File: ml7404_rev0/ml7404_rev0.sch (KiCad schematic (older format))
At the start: 97 parts, among them CN1 MHF-SW23, 20549-001E, CN2 MHF1, 20279-001E-03, U1 SKY13438-374LF, U2 ML7404, U3 BRCB032GWZ-3, U4 BH18PB1WFV

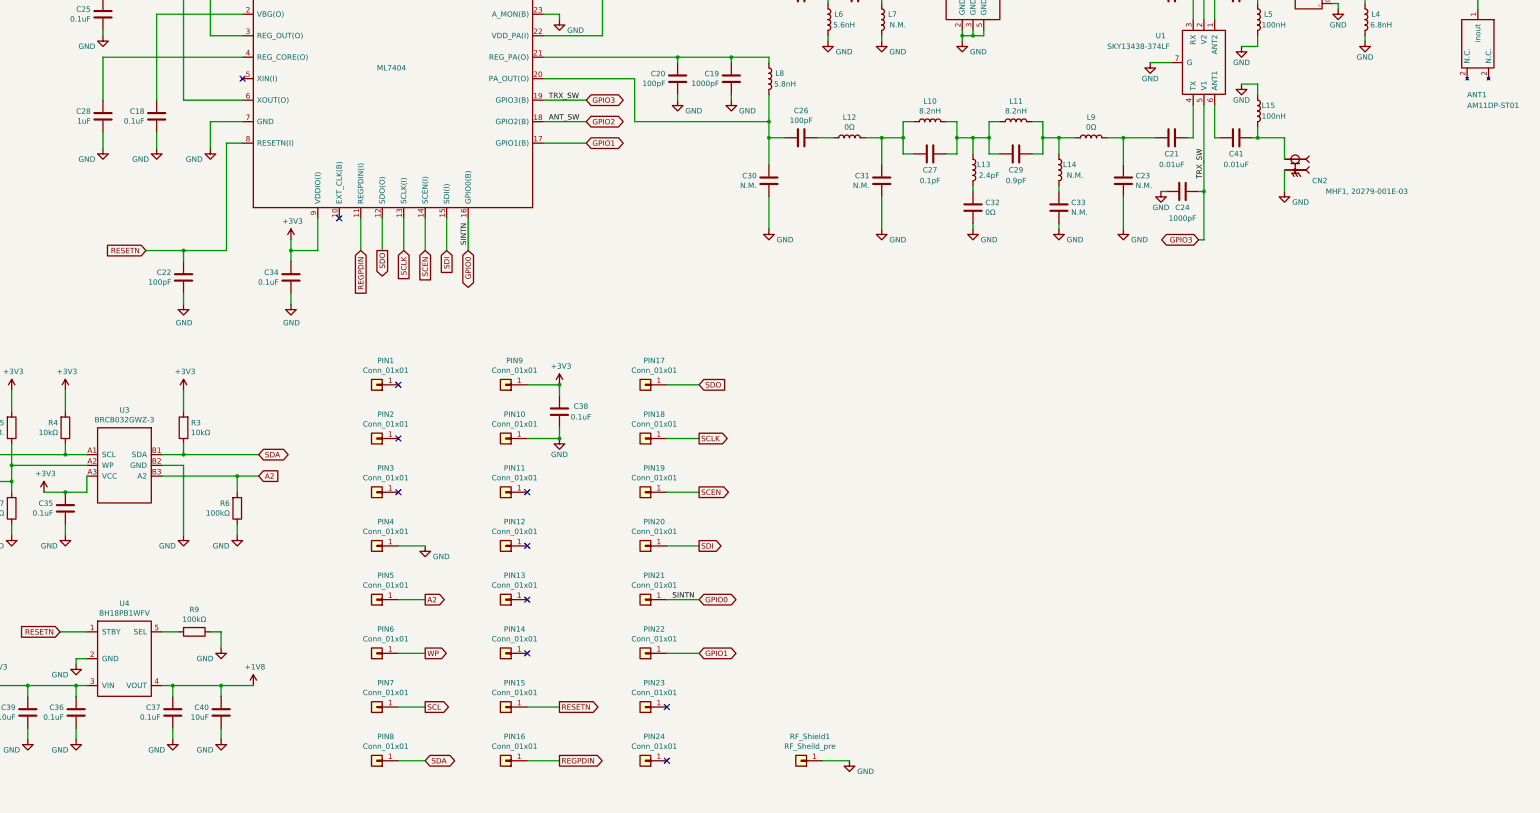
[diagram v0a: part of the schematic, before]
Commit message: adjusted RF shield footprint
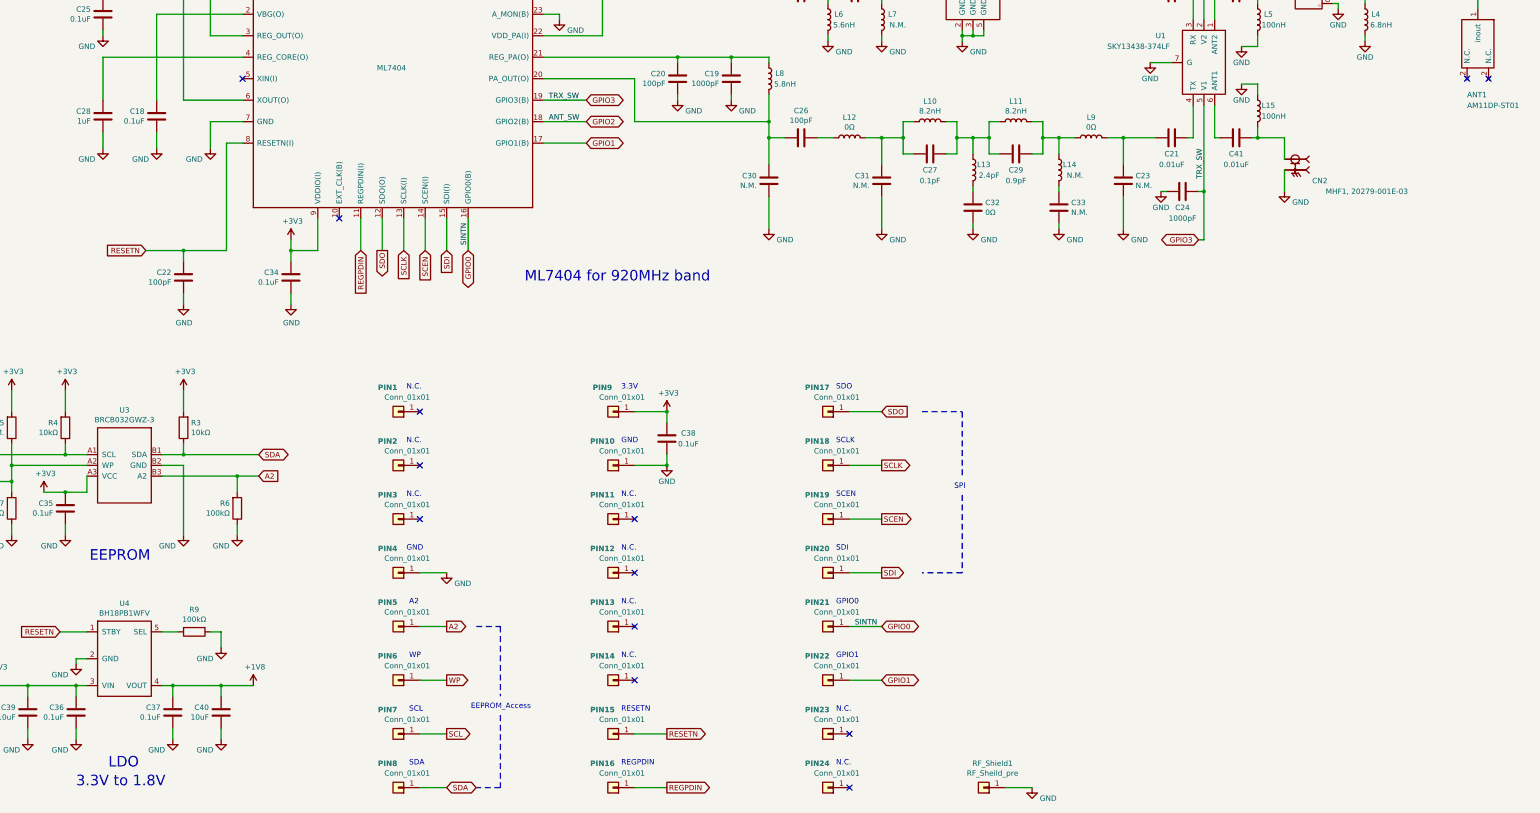
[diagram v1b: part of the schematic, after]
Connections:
- no-connect marks 11 -> 13
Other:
- note added: "3.3V"
- note added: "3.3V to 1.8V"
- note added: "A2"
- note added: "EEPROM"
- note added: "EEPROM_Access"
- note added: "GND"
- note added: "GPIO0"
- note added: "GPIO1"
- note added: "LDO"
- note added: "ML7404 for 920MHz band"
- note added: "N.C."
- note added: "REGPDIN"
- note added: "RESETN"
- note added: "SCEN"
- note added: "SCL"
- note added: "SCLK"
- note added: "SDA"
- note added: "SDI"
- note added: "SDO"
- note added: "SPI"
- note added: "WP"
- moved on the sheet: C38, PIN1, PIN10, PIN11, PIN12, PIN13, PIN14, PIN15, PIN16, PIN17, PIN18, PIN19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

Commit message: pre layout2
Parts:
- removed CN1: MHF-SW23, 20549-001E, ml7404_module:IPEX_20549-001E, symbol ml7404_module:20549-001E
- removed PIN21, PIN22, PIN23, PIN24: Conn_01x01, ml7404_module:terminal, symbol Connector_Generic:Conn_01x01
- removed R3, R4, R7: 10kΩ, Resistor_SMD:R_0402_1005Metric, symbol Device:R
- removed RF_Shield1: RF_Sheild_pre, ml7404_module:RF_Shield_pre_29.85x24.0mm, symbol Connector_Generic:Conn_01x01
- removed U3: BRCB032GWZ-3, ml7404_module:BRCB032GWZ-3, symbol ml7404_module:BRCB032GWZ-3
- added CL1, CL2: UTC(RF_Shield_Clip), ml7404_module:UTC_RF_Shield_Clip, symbol Connector_Generic:Conn_01x03
- added RF_shield1: 1500_RF_shield_soldered_recess, ml7404_module:1500_RF_Shield_soldered_30mmx25mm, symbol Connector_Generic:Conn_01x01
- added U3: BR24GxxNUXxx, ml7404_module:BR24GxxNUXxx, symbol ml7404_module:BR24GxxNUXxx
- C1, C10, C11, C12, C13, C14, C15, C16, C17, C18, C19, C2, C20, C21, C22, C23, C24, C25, C26, C27, C28, C29, C3, C30, C31, C32, C33, C34, C35, C36, C37, C38, C4, C41, C5, C6, C7, C8, C9: footprint Capacitor_SMD:C_0402_1005Metric -> ml7404_module:C_0402_1005Metric
- C39, C40: footprint Capacitor_SMD:C_0603_1608Metric -> ml7404_module:C_0603_1608Metric
- L1, L10, L11, L12, L13, L14, L15, L2, L3, L4, L5, L6, L7, L8, L9: footprint Inductor_SMD:L_0402_1005Metric -> ml7404_module:L_0402_1005Metric
- R1, R6, R9: footprint Resistor_SMD:R_0402_1005Metric -> ml7404_module:R_0402_1005Metric
- R5: value N.M. -> 10kΩ; footprint Resistor_SMD:R_0402_1005Metric -> ml7404_module:R_0402_1005Metric
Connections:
- net +3V3: now also U3.8 (VCC)
- net A2: now also U3.3 (A2)
- net GND: now also PIN1.1 (Pin_1), PIN11.1 (Pin_1), PIN20.1 (Pin_1), CL1.1 (Pin_1), CL1.2 (Pin_2), CL1.3 (Pin_3), CL2.1 (Pin_1), CL2.2 (Pin_2), CL2.3 (Pin_3), RF_shield1.1 (Pin_1), U3.1 (A0), U3.2 (A1), U3.4 (GND), U3.9 (GND)
- net GPIO0: now also PIN18.1 (Pin_1)
- net GPIO1: now also PIN19.1 (Pin_1)
- net REGPDIN: now also PIN13.1 (Pin_1); no longer PIN16.1 (Pin_1)
- net RESETN: now also PIN12.1 (Pin_1); no longer PIN15.1 (Pin_1)
- net SCEN: now also PIN16.1 (Pin_1); no longer PIN19.1 (Pin_1)
- net SCL: now also PIN8.1 (Pin_1), U3.6 (SCL); no longer PIN7.1 (Pin_1)
- net SCLK: now also PIN15.1 (Pin_1); no longer PIN18.1 (Pin_1)
- net SDA: now also PIN7.1 (Pin_1), U3.5 (SDA); no longer PIN8.1 (Pin_1)
- net SDI: now also PIN17.1 (Pin_1); no longer PIN20.1 (Pin_1)
- net SDO: now also PIN14.1 (Pin_1); no longer PIN17.1 (Pin_1)
- net WP: now also U3.7 (WP)
- net at C8.1, L5.1: now also L2.1, L4.1
- no-connect marks 13 -> 6
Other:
- moved on the sheet: C35, C38, PIN1, PIN10, PIN11, PIN12, PIN13, PIN14, PIN15, PIN16, PIN2, PIN3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

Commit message: Change RF SMD size 0603
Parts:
- C14, C15, C16, C17, C19, C20, C21, C23, C24, C26, C27, C29, C30, C31, C32, C33, C41, C8: footprint ml7404_module:C_0402_1005Metric -> ml7404_module:C_0201_0603Metric
- L10, L11, L12, L13, L14, L15, L2, L3, L4, L5, L6, L7, L8, L9: footprint ml7404_module:L_0402_1005Metric -> ml7404_module:L_0201_0603Metric
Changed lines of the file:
@@
 F 0 "C20" H 7736 4104 50  0000 R CNN
 F 1 "100pF" H 7736 4195 50  0000 R CNN
-F 2 "ml7404_module:C_0402_1005Metric" H 7888 4000 50  0001 C CNN
+F 2 "ml7404_module:C_0201_0603Metric" H 7888 4000 50  0001 C CNN
 F 3 "~" H 7850 4150 50  0001 C CNN
 	1    7850 4150
@@
 F 0 "C19" H 8236 4104 50  0000 R CNN
 F 1 "1000pF" H 8236 4195 50  0000 R CNN
-F 2 "ml7404_module:C_0402_1005Metric" H 8388 4000 50  0001 C CNN
+F 2 "ml7404_module:C_0201_0603Metric" H 8388 4000 50  0001 C CNN
 F 3 "~" H 8350 4150 50  0001 C CNN
 	1    8350 4150
@@
 F 0 "L8" H 8800 4200 50  0000 C CNN
 F 1 "5.8nH" H 8850 4100 50  0000 C CNN
-F 2 "ml7404_module:L_0402_1005Metric" H 8700 4150 50  0001 C CNN
+F 2 "ml7404_module:L_0201_0603Metric" H 8700 4150 50  0001 C CNN
 F 3 "~" H 8700 4150 50  0001 C CNN
 	1    8700 4150
@@
 F 0 "C30" H 8586 5054 50  0000 R CNN
 F 1 "N.M." H 8586 5145 50  0000 R CNN
-F 2 "ml7404_module:C_0402_1005Metric" H 8738 4950 50  0001 C CNN
+F 2 "ml7404_module:C_0201_0603Metric" H 8738 4950 50  0001 C CNN
 F 3 "~" H 8700 5100 50  0001 C CNN
 	1    8700 5100
@@
 F 0 "C26" V 8748 4700 50  0000 C CNN
 F 1 "100pF" V 8839 4700 50  0000 C CNN
-F 2 "ml7404_module:C_0402_1005Metric" H 9038 4550 50  0001 C CNN
+F 2 "ml7404_module:C_0201_0603Metric" H 9038 4550 50  0001 C CNN
 F 3 "~" H 9000 4700 50  0001 C CNN
 	1    9000 4700
@@
 F 0 "L12" V 9640 4700 50  0000 C CNN
 F 1 "0Ω" V 9549 4700 50  0000 C CNN
-F 2 "ml7404_module:L_0402_1005Metric" H 9450 4700 50  0001 C CNN
+F 2 "ml7404_module:L_0201_0603Metric" H 9450 4700 50  0001 C CNN
 F 3 "~" H 9450 4700 50  0001 C CNN
 	1    9450 4700
@@
 F 0 "C31" H 9636 5054 50  0000 R CNN
 F 1 "N.M." H 9636 5145 50  0000 R CNN
-F 2 "ml7404_module:C_0402_1005Metric" H 9788 4950 50  0001 C CNN
+F 2 "ml7404_module:C_0201_0603Metric" H 9788 4950 50  0001 C CNN
 F 3 "~" H 9750 5100 50  0001 C CNN
 	1    9750 5100
@@
 F 0 "L13" H 10700 5050 50  0000 C CNN
 F 1 "2.4pF" H 10750 4950 50  0000 C CNN
-F 2 "ml7404_module:L_0402_1005Metric" H 10600 5000 50  0001 C CNN
+F 2 "ml7404_module:L_0201_0603Metric" H 10600 5000 50  0001 C CNN
 F 3 "~" H 10600 5000 50  0001 C CNN
 	1    10600 5000
@@
 F 0 "C32" H 10486 5304 50  0000 R CNN
 F 1 "0Ω" H 10486 5395 50  0000 R CNN
-F 2 "ml7404_module:C_0402_1005Metric" H 10638 5200 50  0001 C CNN
+F 2 "ml7404_module:C_0201_0603Metric" H 10638 5200 50  0001 C CNN
 F 3 "~" H 10600 5350 50  0001 C CNN
 	1    10600 5350
@@
 F 0 "L11" V 11190 4550 50  0000 C CNN
 F 1 "8.2nH" V 11099 4550 50  0000 C CNN
-F 2 "ml7404_module:L_0402_1005Metric" H 11000 4550 50  0001 C CNN
+F 2 "ml7404_module:L_0201_0603Metric" H 11000 4550 50  0001 C CNN
 F 3 "~" H 11000 4550 50  0001 C CNN
 	1    11000 4550
@@
 F 0 "C29" V 11150 4850 50  0000 C CNN
 F 1 "0.9pF" V 11250 4850 50  0000 C CNN
-F 2 "ml7404_module:C_0402_1005Metric" H 11038 4700 50  0001 C CNN
+F 2 "ml7404_module:C_0201_0603Metric" H 11038 4700 50  0001 C CNN
 F 3 "~" H 11000 4850 50  0001 C CNN
 	1    11000 4850
@@
 F 0 "L14" H 11500 5050 50  0000 C CNN
 F 1 "N.M." H 11550 4950 50  0000 C CNN
-F 2 "ml7404_module:L_0402_1005Metric" H 11400 5000 50  0001 C CNN
+F 2 "ml7404_module:L_0201_0603Metric" H 11400 5000 50  0001 C CNN
 F 3 "~" H 11400 5000 50  0001 C CNN
 	1    11400 5000
@@
 F 0 "C33" H 11286 5304 50  0000 R CNN
 F 1 "N.M." H 11286 5395 50  0000 R CNN
-F 2 "ml7404_module:C_0402_1005Metric" H 11438 5200 50  0001 C CNN
+F 2 "ml7404_module:C_0201_0603Metric" H 11438 5200 50  0001 C CNN
 F 3 "~" H 11400 5350 50  0001 C CNN
 	1    11400 5350
@@
 F 0 "C27" V 10350 4850 50  0000 C CNN
 F 1 "0.1pF" V 10450 4850 50  0000 C CNN
-F 2 "ml7404_module:C_0402_1005Metric" H 10238 4700 50  0001 C CNN
+F 2 "ml7404_module:C_0201_0603Metric" H 10238 4700 50  0001 C CNN
 F 3 "~" H 10200 4850 50  0001 C CNN
 	1    10200 4850
@@
 F 0 "L10" V 10390 4550 50  0000 C CNN
 F 1 "8.2nH" V 10299 4550 50  0000 C CNN
-F 2 "ml7404_module:L_0402_1005Metric" H 10200 4550 50  0001 C CNN
+F 2 "ml7404_module:L_0201_0603Metric" H 10200 4550 50  0001 C CNN
 F 3 "~" H 10200 4550 50  0001 C CNN
 	1    10200 4550
@@
 F 0 "L9" V 11890 4700 50  0000 C CNN
 F 1 "0Ω" V 11799 4700 50  0000 C CNN
-F 2 "ml7404_module:L_0402_1005Metric" H 11700 4700 50  0001 C CNN
+F 2 "ml7404_module:L_0201_0603Metric" H 11700 4700 50  0001 C CNN
 F 3 "~" H 11700 4700 50  0001 C CNN
 	1    11700 4700
@@
 F 0 "C23" H 11886 5054 50  0000 R CNN
 F 1 "N.M." H 11886 5145 50  0000 R CNN
-F 2 "ml7404_module:C_0402_1005Metric" H 12038 4950 50  0001 C CNN
+F 2 "ml7404_module:C_0201_0603Metric" H 12038 4950 50  0001 C CNN
 F 3 "~" H 12000 5100 50  0001 C CNN
 	1    12000 5100
@@
 F 0 "C16" V 8748 3350 50  0000 C CNN
 F 1 "0Ω" V 8839 3350 50  0000 C CNN
-F 2 "ml7404_module:C_0402_1005Metric" H 9038 3200 50  0001 C CNN
+F 2 "ml7404_module:C_0201_0603Metric" H 9038 3200 50  0001 C CNN
 F 3 "~" H 9000 3350 50  0001 C CNN
 	1    9000 3350
@@
 F 0 "L6" H 9350 3650 50  0000 C CNN
 F 1 "5.6nH" H 9400 3550 50  0000 C CNN
-F 2 "ml7404_module:L_0402_1005Metric" H 9250 3600 50  0001 C CNN
+F 2 "ml7404_module:L_0201_0603Metric" H 9250 3600 50  0001 C CNN
 F 3 "~" H 9250 3600 50  0001 C CNN
 	1    9250 3600
@@
 F 0 "C17" V 9248 3350 50  0000 C CNN
 F 1 "3.9pF" V 9339 3350 50  0000 C CNN
-F 2 "ml7404_module:C_0402_1005Metric" H 9538 3200 50  0001 C CNN
+F 2 "ml7404_module:C_0201_0603Metric" H 9538 3200 50  0001 C CNN
 F 3 "~" H 9500 3350 50  0001 C CNN
 	1    9500 3350
@@
 F 0 "L7" H 9850 3650 50  0000 C CNN
 F 1 "N.M." H 9900 3550 50  0000 C CNN
-F 2 "ml7404_module:L_0402_1005Metric" H 9750 3600 50  0001 C CNN
+F 2 "ml7404_module:L_0201_0603Metric" H 9750 3600 50  0001 C CNN
 F 3 "~" H 9750 3600 50  0001 C CNN
 	1    9750 3600
@@
 F 0 "C14" V 12198 3350 50  0000 C CNN
 F 1 "0.01uF" V 12289 3350 50  0000 C CNN
-F 2 "ml7404_module:C_0402_1005Metric" H 12488 3200 50  0001 C CNN
+F 2 "ml7404_module:C_0201_0603Metric" H 12488 3200 50  0001 C CNN
 F 3 "~" H 12450 3350 50  0001 C CNN
 	1    12450 3350
@@
 F 0 "C21" V 12600 4700 50  0000 C CNN
 F 1 "0.01uF" V 12700 4700 50  0000 C CNN
-F 2 "ml7404_module:C_0402_1005Metric" H 12488 4550 50  0001 C CNN
+F 2 "ml7404_module:C_0201_0603Metric" H 12488 4550 50  0001 C CNN
 F 3 "~" H 12450 4700 50  0001 C CNN
 	1    12450 4700
@@
 F 0 "C8" V 12798 3350 50  0000 C CNN
 F 1 "0.01uF" V 12889 3350 50  0000 C CNN
-F 2 "ml7404_module:C_0402_1005Metric" H 13088 3200 50  0001 C CNN
+F 2 "ml7404_module:C_0201_0603Metric" H 13088 3200 50  0001 C CNN
 F 3 "~" H 13050 3350 50  0001 C CNN
 	1    13050 3350
@@
 F 0 "C41" V 13200 4700 50  0000 C CNN
 F 1 "0.01uF" V 13300 4700 50  0000 C CNN
-F 2 "ml7404_module:C_0402_1005Metric" H 13088 4550 50  0001 C CNN
+F 2 "ml7404_module:C_0201_0603Metric" H 13088 4550 50  0001 C CNN
 F 3 "~" H 13050 4700 50  0001 C CNN
 	1    13050 4700
@@
 F 0 "L15" H 13350 4500 50  0000 C CNN
 F 1 "100nH" H 13400 4400 50  0000 C CNN
-F 2 "ml7404_module:L_0402_1005Metric" H 13250 4450 50  0001 C CNN
+F 2 "ml7404_module:L_0201_0603Metric" H 13250 4450 50  0001 C CNN
 F 3 "~" H 13250 4450 50  0001 C CNN
 	1    13250 4450
@@
 F 0 "L5" H 13350 3650 50  0000 C CNN
 F 1 "100nH" H 13400 3550 50  0000 C CNN
-F 2 "ml7404_module:L_0402_1005Metric" H 13250 3600 50  0001 C CNN
+F 2 "ml7404_module:L_0201_0603Metric" H 13250 3600 50  0001 C CNN
 F 3 "~" H 13250 3600 50  0001 C CNN
 	1    13250 3600
@@
 F 0 "C24" V 12700 5200 50  0000 C CNN
 F 1 "1000pF" V 12800 5200 50  0000 C CNN
-F 2 "ml7404_module:C_0402_1005Metric" H 12588 5050 50  0001 C CNN
+F 2 "ml7404_module:C_0201_0603Metric" H 12588 5050 50  0001 C CNN
 F 3 "~" H 12550 5200 50  0001 C CNN
 	1    12550 5200
@@
 F 0 "C15" V 12298 2850 50  0000 C CNN
 F 1 "1000pF" V 12389 2850 50  0000 C CNN
-F 2 "ml7404_module:C_0402_1005Metric" H 12588 2700 50  0001 C CNN
+F 2 "ml7404_module:C_0201_0603Metric" H 12588 2700 50  0001 C CNN
 F 3 "~" H 12550 2850 50  0001 C CNN
 	1    12550 2850
@@
 F 0 "L4" H 14350 3650 50  0000 C CNN
 F 1 "6.8nH" H 14400 3550 50  0000 C CNN
-F 2 "ml7404_module:L_0402_1005Metric" H 14250 3600 50  0001 C CNN
+F 2 "ml7404_module:L_0201_0603Metric" H 14250 3600 50  0001 C CNN
 F 3 "~" H 14250 3600 50  0001 C CNN
 	1    14250 3600
@@
 F 0 "L2" V 14740 3350 50  0000 C CNN
 F 1 "39nH" V 14649 3350 50  0000 C CNN
-F 2 "ml7404_module:L_0402_1005Metric" H 14550 3350 50  0001 C CNN
+F 2 "ml7404_module:L_0201_0603Metric" H 14550 3350 50  0001 C CNN
 F 3 "~" H 14550 3350 50  0001 C CNN
 	1    14550 3350
@@
 F 0 "L3" V 15190 3350 50  0000 C CNN
 F 1 "2.2nH" V 15099 3350 50  0000 C CNN
-F 2 "ml7404_module:L_0402_1005Metric" H 15000 3350 50  0001 C CNN
+F 2 "ml7404_module:L_0201_0603Metric" H 15000 3350 50  0001 C CNN
 F 3 "~" H 15000 3350 50  0001 C CNN
 	1    15000 3350
